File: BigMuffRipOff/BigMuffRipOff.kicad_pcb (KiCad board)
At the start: 4 copper layers, 105 x 45.5 mm, 78 parts, among them J1 284697-E, J2 NMJ6HFD2, J3 NMJ6HFD2, J4 2125201004, J5 PJ-007, J6 2125201004, J7 2125201004, Q1 BC549, Q2 BC549, Q3 BC549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

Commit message: datasheet updates
womp womp
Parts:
- removed G***: LOGO, LOGO
- moved J3 165.0 mm to (35.8, 96.7), turned to 0 degrees
- moved H4 153.1 mm to (56.8, 94.0)
- moved H2 148.5 mm to (56.8, 82.1)
- moved C20 138.7 mm to (43.0, 133.5), turned to 0 degrees
- moved J5 137.5 mm to (39.5, 120.7), turned to 0 degrees
- moved C19 135.8 mm to (43.0, 131.0)
- moved U10 132.7 mm to (32.0, 132.0), turned to 0 degrees
- moved U6 130.8 mm to (45.9, 119.6), turned to 0 degrees
- moved C17 124.7 mm to (80.1, 71.7), turned to 0 degrees
- moved C14 120.6 mm to (43.0, 126.0), turned to 0 degrees
- moved C15 117.6 mm to (43.0, 128.5)
- moved U5 114.4 mm to (83.0, 85.5), turned to 0 degrees
- moved J4 112.2 mm to (35.5, 69.4), turned to 0 degrees
- moved Q4 111.5 mm to (69.5, 81.1), turned to 0 degrees
- moved J6 110.9 mm to (48.1, 69.4), turned to 0 degrees
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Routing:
- net /Effect Stage/input_signal: track 103.8 -> 0.00 mm
- net /Effect Stage/SPI_MISO: track 99.2 -> 0.00 mm, vias 6 -> 0
- net /Effect Stage/SPI_CLK: track 85.3 -> 0.00 mm, vias 5 -> 0
- net /Effect Stage/CS_3: track 64.6 -> 0.00 mm, vias 2 -> 0
- net /Effect Stage/CS_4: track 61.3 -> 0.00 mm, vias 4 -> 0
- net /Effect Stage/CS_2: track 40.1 -> 0.00 mm, vias 4 -> 0
- net /MCU/LDO_EN: track 38.9 -> 0.00 mm, vias 2 -> 0
- net /MCU/RST: track 37.0 -> 0.00 mm, vias 2 -> 0
- net /MCU/SWIM: track 30.4 -> 0.00 mm, vias 2 -> 0
- net /MCU/Pot_3: track 29.9 -> 0.00 mm, vias 2 -> 0
- net 9V: track 27.7 -> 0.00 mm, vias 12 -> 0
- net Net-(Q3-C): track 26.7 -> 0.00 mm
- net /MCU/Pot_2: track 23.9 -> 0.00 mm, vias 2 -> 0
- net /Effect Stage/CS_1: track 19.3 -> 0.00 mm, vias 2 -> 0
- net Net-(U3-L): track 19.0 -> 0.00 mm
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- removed copper zone on In2.Cu, net 3.3V
- removed copper zone on In2.Cu, net 4.5V
- removed copper zone on In2.Cu, net 9V
- removed copper zone on F.Cu, net GND
- removed copper zone on In1.Cu, net GND
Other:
- board outline removed

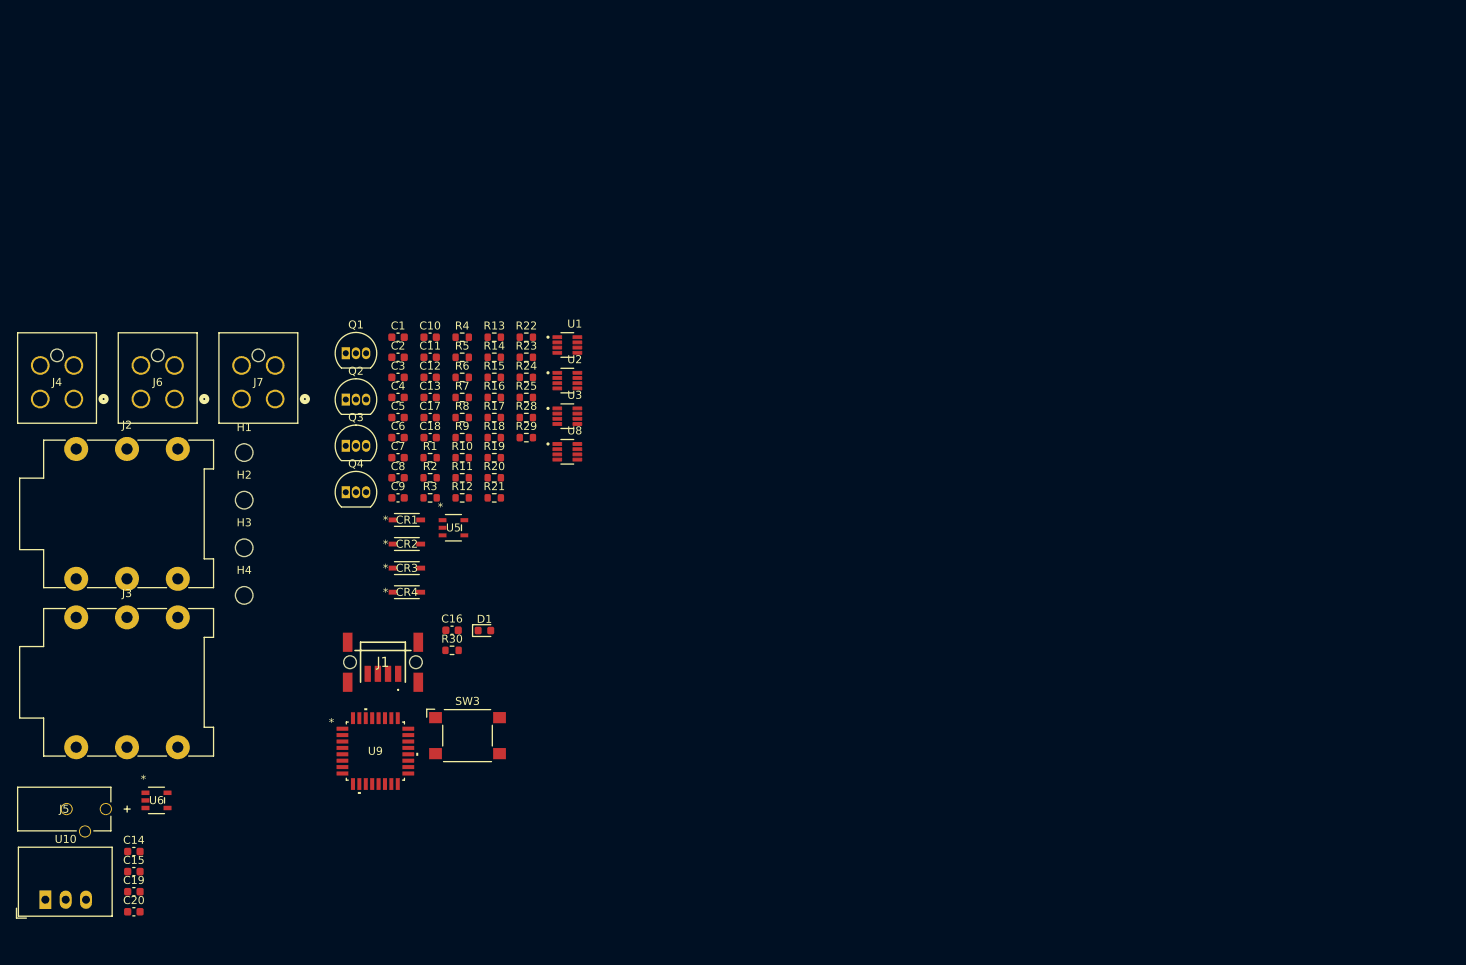
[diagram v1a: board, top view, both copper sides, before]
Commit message: starting to redo board layout
also finished changing the schematic
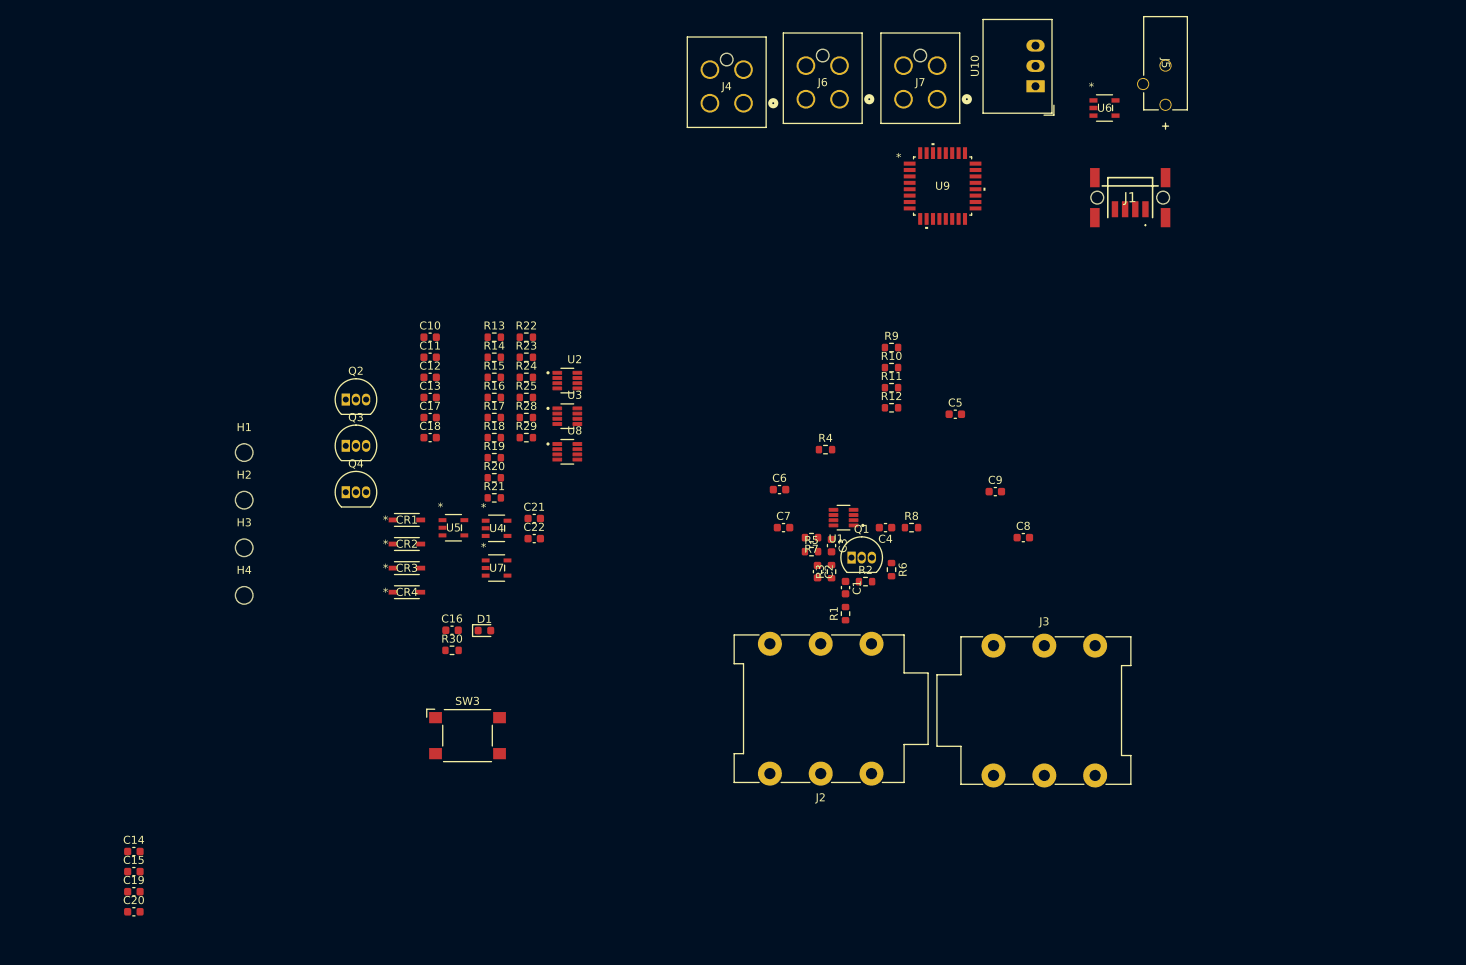
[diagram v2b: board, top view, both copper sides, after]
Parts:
- added C21: 0.1u, Capacitor_SMD:C_0603_1608Metric, F.Cu at (93.1, 84.4)
- added C22: 0.1u, Capacitor_SMD:C_0603_1608Metric, F.Cu at (93.1, 86.9)
- added U4: TL071HIDBVR, 284867-E-footprint:SOT23_DBV_5_TEX, F.Cu at (88.4, 85.6)
- added U7: TL071HIDBVR, 284867-E-footprint:SOT23_DBV_5_TEX, F.Cu at (88.4, 90.5)
- R23: value 5k -> 10k
- R24: value 10k -> 20k
- moved U10 160.2 mm to (155.8, 30.3), turned to 90 degrees
- moved J5 159.0 mm to (172.0, 32.6), turned to -90 degrees
- moved U6 146.7 mm to (164.4, 33.0)
- moved J3 114.7 mm to (150.5, 100.2)
- moved J1 110.0 mm to (167.6, 44.2)
- moved J2 107.4 mm to (135.2, 116.2), turned to 180 degrees
- moved U9 100.1 mm to (144.1, 42.8)
- moved J4 91.5 mm to (119.2, 32.4)
- moved J6 91.2 mm to (131.2, 31.9)
- moved J7 90.8 mm to (143.4, 31.9)
- moved C8 78.5 mm to (154.2, 86.8)
- moved C9 74.7 mm to (150.7, 81.0)
- moved C5 69.7 mm to (145.7, 71.3)
- moved Q1 68.2 mm to (132.8, 89.2)
- moved C1 64.1 mm to (132.0, 93.0), turned to -90 degrees
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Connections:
- C13 pad 1: Net-(C13-Pad1) -> Net-(U8-H)
- C18 pad 1: Net-(C18-Pad1) -> Net-(U3-H)
- R23 pad 1: Net-(C18-Pad1) -> Net-(U7-IN-)
- R23 pad 2: Net-(U3-W) -> Net-(U5-IN-)
- R24 pad 1: Net-(C13-Pad1) -> Net-(U5-IN-)
- R24 pad 2: Net-(U8-W) -> Net-(U4-IN-)
- R25 pad 1: Net-(U3-L) -> Net-(U5-IN-)
- U3 pad 2: 9V -> 4.5V
- U3 pad 3: 4.5V -> GND
- U3 pad 7: Net-(U3-L) -> GND
- U3 pad 8: unconnected-(U3-H-Pad8) -> Net-(U3-H)
- U5 pad 4: Net-(U3-L) -> Net-(U5-IN-)
- U8 pad 2: 9V -> 4.5V
- U8 pad 3: 4.5V -> GND
- U8 pad 7: Net-(U3-L) -> GND
- U8 pad 8: unconnected-(U8-H-Pad8) -> Net-(U8-H)

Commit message: did half of the changes
gonna finish the next have next time
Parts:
- removed R28, R29: 30k, Resistor_SMD:R_0603_1608Metric
- moved Q4 98.5 mm to (167.5, 91.1), turned to 180 degrees
- moved C13 92.8 mm to (170.0, 92.2), turned to 90 degrees
- moved C12 89.3 mm to (167.2, 86.2)
- moved Q3 86.4 mm to (155.2, 86.0), turned to -90 degrees
- moved C17 85.7 mm to (161.0, 100.0), turned to 180 degrees
- moved C10 83.9 mm to (160.5, 85.8), turned to 180 degrees
- moved R22 83.5 mm to (170.8, 89.8), turned to 180 degrees
- moved C11 83.2 mm to (161.5, 81.5), turned to 90 degrees
- moved R20 81.1 mm to (168.8, 88.0), turned to 180 degrees
- moved CR2 79.1 mm to (156.0, 81.0)
- moved CR1 78.8 mm to (156.0, 83.2), turned to 180 degrees
- moved R19 78.2 mm to (165.5, 88.0)
- moved Q2 76.5 mm to (144.2, 86.0), turned to -90 degrees
- moved U5 74.9 mm to (156.8, 98.8), turned to 180 degrees
- moved R18 74.5 mm to (161.2, 88.2), turned to 90 degrees
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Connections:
- U1 pad 5: /Effect Stage/SPI_MISO -> /Effect Stage/SPI_MOSI
- U2 pad 5: /Effect Stage/SPI_MISO -> /Effect Stage/SPI_MOSI
- U3 pad 5: /Effect Stage/SPI_MISO -> /Effect Stage/SPI_MOSI
- U4 pad 2: unconnected-(U4-V--Pad2) -> GND
- U8 pad 5: /Effect Stage/SPI_MISO -> /Effect Stage/SPI_MOSI
- U9 pad 13: /Effect Stage/SPI_CLK -> unconnected-(U9A-PB0-Pad13)
- U9 pad 14: /Effect Stage/SPI_MISO -> /Effect Stage/CS_1
- U9 pad 16: /Effect Stage/CS_3 -> /Effect Stage/CS_2
- U9 pad 17: /Effect Stage/CS_2 -> /Effect Stage/CS_3
- U9 pad 18: /Effect Stage/CS_1 -> /Effect Stage/SPI_CLK
- U9 pad 19: unconnected-(U9A-PB6-Pad19) -> /MCU/SPI_MOSI
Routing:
- net /Effect Stage/input_signal: track 0.00 -> 28.2 mm
- net Net-(Q3-C): track 0.00 -> 17.3 mm
- net Net-(Q2-C): track 0.00 -> 16.7 mm
- net Net-(Q3-B): track 0.00 -> 10.1 mm
- net Net-(Q2-B): track 0.00 -> 10.1 mm
- net Net-(Q1-B): track 0.00 -> 8.51 mm
- net Net-(U5-OUT): track 0.00 -> 7.18 mm
- net Net-(Q4-B): track 0.00 -> 6.57 mm
- net /Effect Stage/output_signal: track 0.00 -> 6.38 mm
- net Net-(U2-H): track 0.00 -> 6.18 mm
- net Net-(U5-IN-): track 0.00 -> 5.86 mm
- net Net-(U4-IN-): track 0.00 -> 5.67 mm
- net Net-(U7-IN-): track 0.00 -> 5.57 mm
- net Net-(U2-L): track 0.00 -> 5.54 mm
- net Net-(Q4-C): track 0.00 -> 4.53 mm
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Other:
- board outline added: 50.9 x 74 mm

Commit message: getting closer on finishing layout
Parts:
- added C23: 0.1u, Capacitor_SMD:C_0603_1608Metric, F.Cu at (144.2, 94.0)
- added C24: 0.1u, Capacitor_SMD:C_0603_1608Metric, F.Cu at (170.5, 84.8)
- added C25: 0.1u, Capacitor_SMD:C_0603_1608Metric, F.Cu at (161.8, 96.8)
- added C26: 0.1u, Capacitor_SMD:C_0603_1608Metric, F.Cu at (137.3, 83.8)
- moved SW3 40.6 mm to (171.0, 70.2), turned to -90 degrees
- moved J5 38.0 mm to (131.5, 67.5), turned to 0 degrees
- moved J1 32.7 mm to (161.2, 69.8), turned to -90 degrees
- moved U6 31.6 mm to (130.2, 75.8), turned to -90 degrees
- moved U10 31.3 mm to (140.5, 72.9), turned to 90 degrees
- moved U9 7.50 mm to (149.9, 70.8), turned to -90 degrees
- moved J7 7.03 mm to (163.7, 59.9)
- moved J6 6.29 mm to (151.9, 59.9)
- moved J4 5.74 mm to (140.5, 59.9)
- moved C21 1.00 mm to (161.8, 95.0)
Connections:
- U6 pad 3: /MCU/LDO_EN -> 9V
- U9 pad 14: /Effect Stage/CS_1 -> unconnected-(U9A-PB1-Pad14)
- U9 pad 15: /Effect Stage/CS_4 -> unconnected-(U9A-PB2-Pad15)
- U9 pad 16: /Effect Stage/CS_2 -> unconnected-(U9A-PB3-Pad16)
- U9 pad 17: /Effect Stage/CS_3 -> unconnected-(U9A-PB4-Pad17)
- U9 pad 19: /MCU/SPI_MOSI -> /Effect Stage/SPI_MOSI
- U9 pad 20: unconnected-(U9A-PB7-Pad20) -> /Effect Stage/CS_1
- U9 pad 21: unconnected-(U9A-PD4-Pad21) -> /Effect Stage/CS_4
- U9 pad 22: /MCU/Pot_1 -> /Effect Stage/CS_3
- U9 pad 23: /MCU/Pot_2 -> /Effect Stage/CS_2
- U9 pad 24: /MCU/Pot_3 -> unconnected-(U9A-PD7-Pad24)
- U9 pad 4: unconnected-(U9A-PA4-Pad4) -> /MCU/Pot_1
- U9 pad 5: /MCU/LDO_EN -> /MCU/Pot_2
- U9 pad 6: unconnected-(U9A-PA6-Pad6) -> /MCU/Pot_3
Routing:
- net /Effect Stage/SPI_MOSI: track 0.00 -> 86.5 mm, vias 0 -> 4
- net /Effect Stage/SPI_CLK: track 0.00 -> 79.8 mm, vias 0 -> 8
- net /Effect Stage/CS_3: track 0.00 -> 31.3 mm, vias 0 -> 2
- net /Effect Stage/CS_4: track 0.00 -> 29.7 mm, vias 0 -> 2
- net /Effect Stage/CS_1: track 0.00 -> 28.1 mm, vias 0 -> 2
- net 4.5V: track 0.00 -> 19.4 mm, vias 0 -> 7
- net /Effect Stage/CS_2: track 0.00 -> 19.1 mm, vias 0 -> 2
- net 9V: track 0.00 -> 11.3 mm, vias 0 -> 8
- net GND: track 0.00 -> 10.1 mm, vias 0 -> 16
- net Net-(Q1-C): track 3.41 -> 7.79 mm
- net Net-(U4-IN+): track 4.37 -> 3.37 mm
- net Net-(U8-W): track 2.21 -> 3.21 mm
- added copper zone on In2.Cu, net 3.3V
- added copper zone on In2.Cu, net 4.5V
- added copper zone on In2.Cu, net 9V
- added copper zone on B.Cu, net GND
- added copper zone on F.Cu, net GND
- added copper zone on In1.Cu, net GND

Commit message: please dont break plsplspls
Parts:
- added C27: 10n, Capacitor_SMD:C_0603_1608Metric, F.Cu at (144.5, 64.0)
- added C28: 100n, Capacitor_SMD:C_0603_1608Metric, F.Cu at (144.5, 66.0)
- added C30: 1u, Capacitor_SMD:C_0603_1608Metric, F.Cu at (143.8, 68.5)
- added J8: Conn_01x04, Connector_PinHeader_2.54mm:PinHeader_1x04_P2.54mm_Vertical, F.Cu at (160.5, 73.5)
- moved H2 121.5 mm to (173.2, 47.2)
- moved H4 120.8 mm to (173.2, 126.2)
- moved C15 116.3 mm to (139.5, 63.5), turned to 180 degrees
- moved C19 107.0 mm to (132.8, 72.7), turned to 90 degrees
- moved C20 100.9 mm to (128.8, 80.2), turned to 180 degrees
- moved C14 100.0 mm to (127.8, 72.8), turned to 90 degrees
- moved H3 80.3 mm to (127.5, 126.2)
- moved C16 79.7 mm to (155.2, 65.0)
- moved R30 79.2 mm to (157.8, 75.2), turned to -90 degrees
- moved H1 76.3 mm to (127.5, 47.2)
- moved D1 72.9 mm to (156.0, 75.2), turned to -90 degrees
- moved J7 29.8 mm to (133.9, 59.4)
- moved J4 18.7 mm to (159.2, 59.4)
- moved SW3 13.4 mm to (169.0, 57.0)
- moved J1 7.75 mm to (169.0, 69.7)
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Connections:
- U9 pad 27: unconnected-(U9A-PC2-Pad27) -> /MCU/UART_RX
- U9 pad 28: unconnected-(U9A-PC3-Pad28) -> /MCU/UART_TX
- U9 pad 9: unconnected-(U9B-VLCD-Pad9) -> 3.3V
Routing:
- net /MCU/RST: track 0.00 -> 36.4 mm, vias 0 -> 2
- net /MCU/Pot_3: track 0.00 -> 23.4 mm
- net 9V: track 11.3 -> 28.1 mm
- net 3.3V: track 0.00 -> 16.6 mm, vias 0 -> 6
- net /MCU/SWIM: track 0.00 -> 14.5 mm, vias 0 -> 2
- net /MCU/Pot_2: track 0.00 -> 11.9 mm
- net /MCU/Pot_1: track 0.00 -> 9.21 mm
- net /MCU/UART_RX: track 0.00 -> 7.16 mm
- net /MCU/UART_TX: track 0.00 -> 6.56 mm
- net GND: track 10.1 -> 12.6 mm, vias 16 -> 33
- net Net-(D1-A): track 0.00 -> 1.77 mm
- net 4.5V: track 19.4 -> 21.1 mm, vias 7 -> 8
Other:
- board size 50.9 x 74 mm -> 50.8 x 84 mm

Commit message: no sure
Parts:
- added G***: LOGO, LOGO, F.Cu at (171.0, 79.5)
- added G***: LOGO, LOGO, B.Cu at (148.8, 83.3)
- moved J5 0.25 mm to (131.8, 67.5)
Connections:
- C21 pad 2: Net-(U4-IN+) -> 4.5V
- C22 pad 2: Net-(U7-IN+) -> 4.5V
- U4 pad 3: Net-(U4-IN+) -> 4.5V
- U7 pad 3: Net-(U7-IN+) -> 4.5V
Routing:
- net GND: track 12.6 -> 27.3 mm, vias 33 -> 40
- net 9V: track 28.1 -> 18.0 mm, vias 8 -> 10
- net 4.5V: track 21.1 -> 26.5 mm, vias 8 -> 10
- net Net-(U4-IN+): track 3.37 -> 0.00 mm
- net /MCU/RST: track 36.4 -> 38.9 mm
- net Net-(U7-IN+): track 2.05 -> 0.00 mm
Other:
- board text added: "Marco Yaipen BigMuff RipOff Rev 1.0 February 14, 2026"
- board text added: "{dblquote}Ain't that just the way it goes on{dblquote} -me"

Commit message: look mom i did it
the board is done
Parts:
- added R26: 500k, Resistor_SMD:R_0603_1608Metric, F.Cu at (144.2, 97.5)
- added R27: 500k, Resistor_SMD:R_0603_1608Metric, F.Cu at (158.0, 91.7)
- added R28: 500k, Resistor_SMD:R_0603_1608Metric, F.Cu at (160.0, 97.5)
- moved C25 1.04 mm to (162.5, 97.5), turned to -90 degrees
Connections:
- C21 pad 2: 4.5V -> Net-(U4-IN+)
- C22 pad 2: 4.5V -> Net-(U7-IN+)
- U4 pad 3: 4.5V -> Net-(U4-IN+)
- U5 pad 3: 4.5V -> Net-(U5-IN+)
- U7 pad 3: 4.5V -> Net-(U7-IN+)
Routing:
- net Net-(U4-IN+): track 0.00 -> 5.52 mm
- net Net-(U7-IN+): track 0.00 -> 4.58 mm
- net Net-(U5-IN+): track 0.00 -> 2.10 mm
- net GND: track 27.3 -> 29.2 mm, vias 40 -> 42
- net 4.5V: track 26.5 -> 25.1 mm
